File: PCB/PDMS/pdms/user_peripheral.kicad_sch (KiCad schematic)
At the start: 11 parts, among them IC12 TMP126NDCKR, IC14 TMP126NDCKR, Q2 MMBT3904

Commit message: Added connector and more
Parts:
- R56, R57: footprint (none) -> Resistor_SMD:R_0402_1005Metric
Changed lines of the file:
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@@
       (effects (font (size 1.27 1.27)) (justify left))
     )
-    (property "Footprint" "" (id 2) (at 59.055 57.785 0)
+    (property "Footprint" "Resistor_SMD:R_0402_1005Metric" (id 2) (at 59.055 57.785 0)
       (effects (font (size 1.27 1.27)) hide)
     )
@@
       (effects (font (size 1.27 1.27)) (justify left))
     )
-    (property "Footprint" "" (id 2) (at 135.255 57.785 0)
-      (effects (font (size 1.27 1.27)) hide)
-    )
+    (property "Footprint" "Resistor_SMD:R_0402_1005Metric" (id 2) (at 135.255 57.785 0)
+      (effects (font (size 1.27 1.27)) hide)
+    )

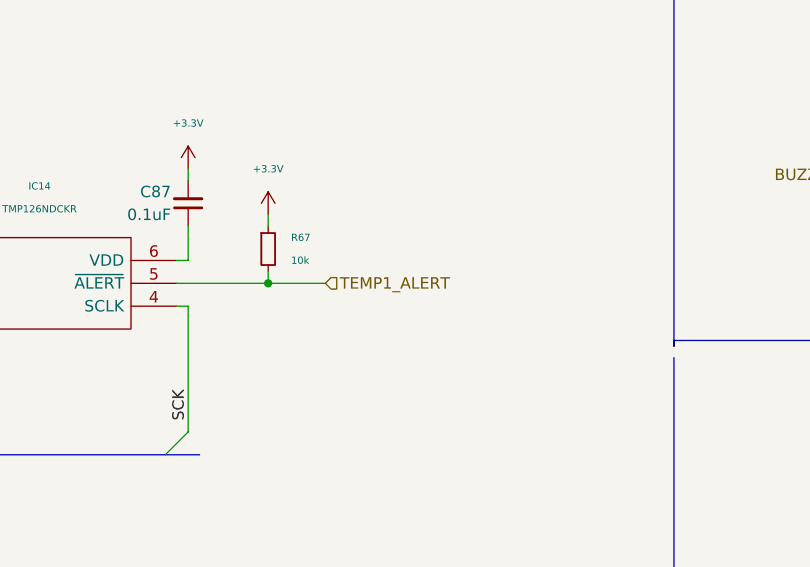
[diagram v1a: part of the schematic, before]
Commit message: Added voltage mux section & layouting high side - hp
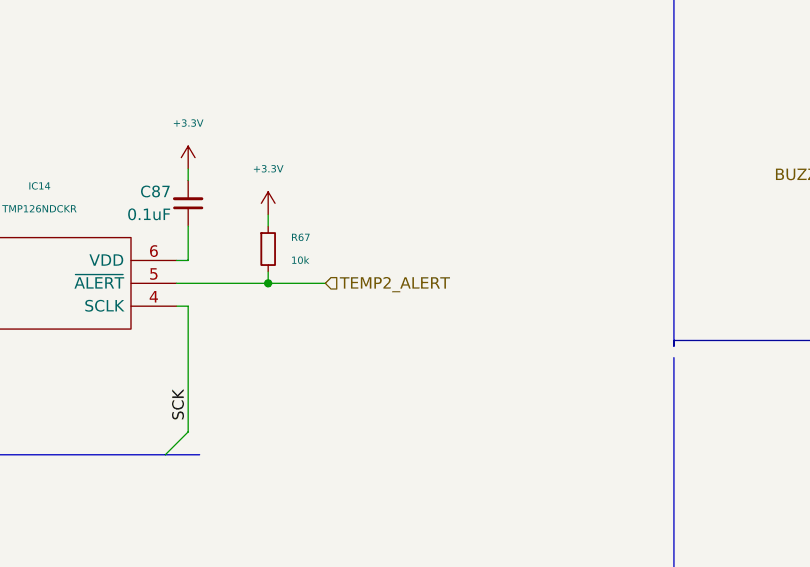
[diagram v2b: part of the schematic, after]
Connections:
- net TEMP1_ALERT: no longer IC14.5 (~{ALERT}), R67.2
- new net TEMP2_ALERT: IC14.5 (~{ALERT}), R67.2
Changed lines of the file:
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@@
     (effects (font (size 1.27 1.27)) (justify right))
   )
-  (hierarchical_label "TEMP1_ALERT" (shape input) (at 184.785 51.435 0)
+  (hierarchical_label "TEMP2_ALERT" (shape input) (at 184.785 51.435 0)
     (effects (font (size 1.27 1.27)) (justify left))
   )

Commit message: Flash layout
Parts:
- C86, C87: footprint Capacitor_SMD:C_0402_1005Metric_Pad0.74x0.62mm_HandSolder -> Capacitor_SMD:C_0402_1005Metric
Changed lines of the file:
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@@
       (effects (font (size 1.27 1.27)) (justify right))
     )
-    (property "Footprint" "Capacitor_SMD:C_0402_1005Metric_Pad0.74x0.62mm_HandSolder" (id 2) (at 169.545 42.545 0)
+    (property "Footprint" "Capacitor_SMD:C_0402_1005Metric" (id 2) (at 169.545 42.545 0)
       (effects (font (size 1.27 1.27)) hide)
     )
@@
       (effects (font (size 1.27 1.27)) (justify right))
     )
-    (property "Footprint" "Capacitor_SMD:C_0402_1005Metric_Pad0.74x0.62mm_HandSolder" (id 2) (at 93.345 42.545 0)
+    (property "Footprint" "Capacitor_SMD:C_0402_1005Metric" (id 2) (at 93.345 42.545 0)
       (effects (font (size 1.27 1.27)) hide)
     )

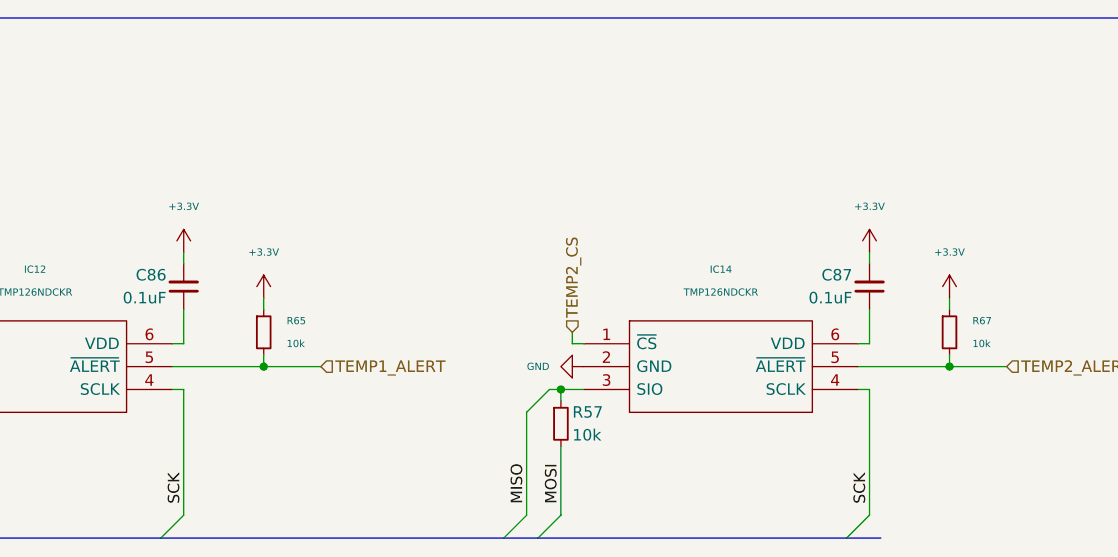
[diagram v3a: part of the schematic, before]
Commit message: ADC protection refactored - 73
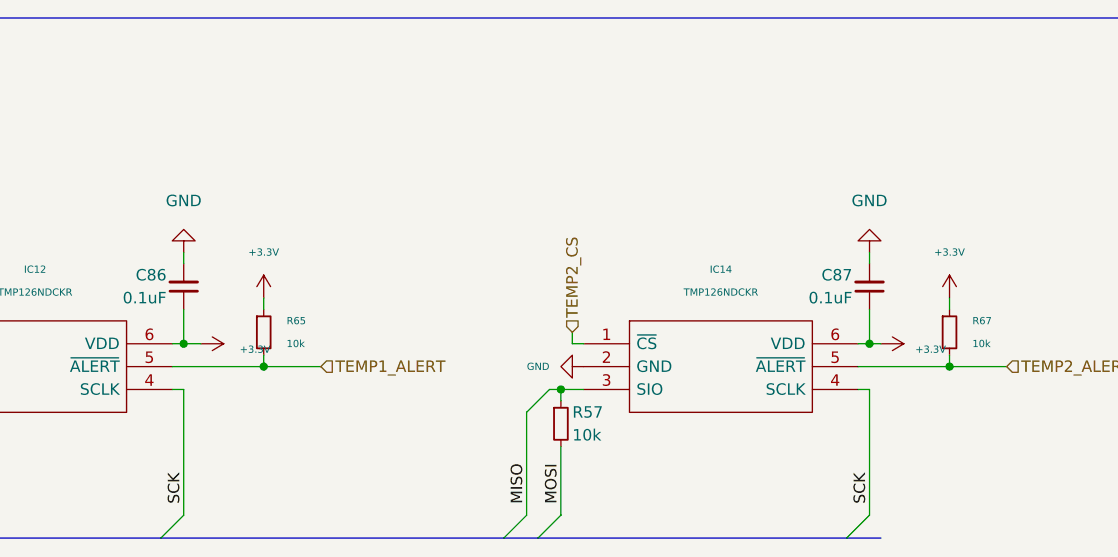
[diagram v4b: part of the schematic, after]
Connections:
- net +3.3V: now also C86.1, C87.1, IC12.6 (VDD), IC14.6 (VDD); no longer C86.2, C87.2
- net GND: now also C86.2, C87.2
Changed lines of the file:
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@@
   (junction (at 59.055 53.975) (diameter 0) (color 0 0 0 0)
   )
+  (junction (at 93.345 48.895) (diameter 0) (color 0 0 0 0)
+  )
   (junction (at 178.435 51.435) (diameter 0) (color 0 0 0 0)
   )
@@
   (junction (at 102.235 51.435) (diameter 0) (color 0 0 0 0)
   )
+  (junction (at 169.545 48.895) (diameter 0) (color 0 0 0 0)
+  )
   (bus_entry (at 128.905 70.485) (size 2.54 -2.54)
     (stroke (width 0) (type default) (color 0 0 0 0))
@@
     (stroke (width 0) (type default) (color 0 0 0 0))
   )
+  (wire (pts (xy 169.545 48.895) (xy 170.815 48.895))
+    (stroke (width 0) (type default) (color 0 0 0 0))
+  )
   (wire (pts (xy 102.235 51.435) (xy 108.585 51.435))
     (stroke (width 0) (type default) (color 0 0 0 0))
@@
   )
   (wire (pts (xy 93.345 53.975) (xy 93.345 67.945))
+    (stroke (width 0) (type default) (color 0 0 0 0))
+  )
+  (wire (pts (xy 93.345 48.895) (xy 95.25 48.895))
     (stroke (width 0) (type default) (color 0 0 0 0))
   )
@@
     (pin "2")
   )
+  (symbol (lib_id "power:GND") (at 169.545 38.735 180) (unit 1)
+    (in_bom yes) (on_board yes) (fields_autoplaced)
+    (property "Reference" "#PWR0309" (id 0) (at 169.545 32.385 0)
+      (effects (font (size 1.27 1.27)) hide)
+    )
+    (property "Value" "GND" (id 1) (at 169.545 33.02 0))
+    (property "Footprint" "" (id 2) (at 169.545 38.735 0)
+      (effects (font (size 1.27 1.27)) hide)
+    )
+    (property "Datasheet" "" (id 3) (at 169.545 38.735 0)
+      (effects (font (size 1.27 1.27)) hide)
+    )
+    (pin "1")
+  )
   (symbol (lib_id "Device:R_Small") (at 59.055 57.785 0) (unit 1)
     (in_bom yes) (on_board yes)
@@
     (pin "2")
   )
-  (symbol (lib_id "power:+3.3V") (at 93.345 38.735 0) (unit 1)
-    (in_bom yes) (on_board yes) (fields_autoplaced)
-    (property "Reference" "#PWR0194" (id 0) (at 93.345 42.545 0)
+  (symbol (lib_id "power:+3.3V") (at 95.25 48.895 270) (unit 1)
+    (in_bom yes) (on_board yes) (fields_autoplaced)
+    (property "Reference" "#PWR0194" (id 0) (at 91.44 48.895 0)
       (effects (font (size 0.8 0.8)) hide)
     )
-    (property "Value" "+3.3V" (id 1) (at 93.345 33.655 0)
-      (effects (font (size 0.8 0.8)))
-    )
+    (property "Value" "+3.3V" (id 1) (at 99.568 49.53 90)
+      (effects (font (size 0.8 0.8)) (justify left))
+    )
+    (property "Footprint" "" (id 2) (at 95.25 48.895 0)
+      (effects (font (size 1.27 1.27)) hide)
+    )
+    (property "Datasheet" "" (id 3) (at 95.25 48.895 0)
+      (effects (font (size 1.27 1.27)) hide)
+    )
+    (pin "1")
+  )
+  (symbol (lib_id "power:+3.3V") (at 170.815 48.895 270) (unit 1)
+    (in_bom yes) (on_board yes) (fields_autoplaced)
+    (property "Reference" "#PWR0233" (id 0) (at 167.005 48.895 0)
+      (effects (font (size 0.8 0.8)) hide)
+    )
+    (property "Value" "+3.3V" (id 1) (at 174.625 49.53 90)
+      (effects (font (size 0.8 0.8)) (justify left))
+    )
+    (property "Footprint" "" (id 2) (at 170.815 48.895 0)
+      (effects (font (size 1.27 1.27)) hide)
+    )
+    (property "Datasheet" "" (id 3) (at 170.815 48.895 0)
+      (effects (font (size 1.27 1.27)) hide)
+    )
+    (pin "1")
+  )
+  (symbol (lib_id "power:GND") (at 93.345 38.735 180) (unit 1)
+    (in_bom yes) (on_board yes) (fields_autoplaced)
+    (property "Reference" "#PWR0310" (id 0) (at 93.345 32.385 0)
+      (effects (font (size 1.27 1.27)) hide)
+    )
+    (property "Value" "GND" (id 1) (at 93.345 33.02 0))
     (property "Footprint" "" (id 2) (at 93.345 38.735 0)
       (effects (font (size 1.27 1.27)) hide)
@@
       (effects (font (size 1.27 1.27)) hide)
     )
-    (pin "1")
-  )
-  (symbol (lib_id "power:+3.3V") (at 169.545 38.735 0) (unit 1)
-    (in_bom yes) (on_board yes) (fields_autoplaced)
-    (property "Reference" "#PWR0233" (id 0) (at 169.545 42.545 0)
-      (effects (font (size 0.8 0.8)) hide)
-    )
-    (property "Value" "+3.3V" (id 1) (at 169.545 33.655 0)
-      (effects (font (size 0.8 0.8)))
-    )
-    (property "Footprint" "" (id 2) (at 169.545 38.735 0)
-      (effects (font (size 1.27 1.27)) hide)
-    )
-    (property "Datasheet" "" (id 3) (at 169.545 38.735 0)
-      (effects (font (size 1.27 1.27)) hide)
-    )

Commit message: PCB finished
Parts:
- removed Q2: MMBT3904, Package_TO_SOT_SMD:SOT-23, symbol Transistor_BJT:MMBT3904
- added Q2: RJU002N06FRAT106, PDMS_Additional:SOT65P210X110-3N, symbol BSPD-07:RJU002N06FRAT106
- BZ1: footprint Buzzer_Beeper:Buzzer_Murata_PKLCS1212E -> Buzzer_Beeper:Buzzer_12x9.5RM7.6
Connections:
- net GND: now also Q2.2
- net at R72.2: now also Q2.1
- net at BZ1.2 (+): now also Q2.3
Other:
- moved on the sheet: BZ1
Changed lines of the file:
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@@
     (stroke (width 0) (type default) (color 0 0 0 0))
   )
-  (wire (pts (xy 243.84 39.37) (xy 245.11 39.37))
+  (wire (pts (xy 243.84 39.624) (xy 245.11 39.624))
     (stroke (width 0) (type default) (color 0 0 0 0))
   )
@@
     (stroke (width 0) (type default) (color 0 0 0 0))
   )
-  (wire (pts (xy 259.08 25.4) (xy 259.08 26.67))
+  (wire (pts (xy 259.08 20.574) (xy 259.08 21.844))
     (stroke (width 0) (type default) (color 0 0 0 0))
   )
@@
     (stroke (width 0) (type default) (color 0 0 0 0))
   )
-  (wire (pts (xy 259.08 31.75) (xy 259.08 34.29))
-    (stroke (width 0) (type default) (color 0 0 0 0))
-  )
   (bus (pts (xy 128.905 70.485) (xy 132.715 70.485))
     (stroke (width 0) (type default) (color 0 0 0 0))
@@
     (stroke (width 0) (type default) (color 0 0 0 0))
   )
-  (wire (pts (xy 250.19 39.37) (xy 251.46 39.37))
+  (wire (pts (xy 250.19 39.624) (xy 251.46 39.624))
+    (stroke (width 0) (type default) (color 0 0 0 0))
+  )
+  (wire (pts (xy 259.08 26.924) (xy 259.08 29.464))
     (stroke (width 0) (type default) (color 0 0 0 0))
   )
@@
     (stroke (width 0) (type default) (color 0 0 0 0))
   )
+  (wire (pts (xy 259.08 44.704) (xy 259.08 48.26))
+    (stroke (width 0) (type default) (color 0 0 0 0))
+  )
   (wire (pts (xy 93.345 48.895) (xy 92.075 48.895))
     (stroke (width 0) (type default) (color 0 0 0 0))
@@
   )
   (polyline (pts (xy 12.065 92.075) (xy 12.065 12.7))
-    (stroke (width 0) (type default) (color 0 0 0 0))
-  )
-  (wire (pts (xy 259.08 44.45) (xy 259.08 48.26))
     (stroke (width 0) (type default) (color 0 0 0 0))
   )
@@
     (effects (font (size 1.27 1.27)) (justify left))
   )
-  (hierarchical_label "BUZZ_IN" (shape input) (at 243.84 39.37 180)
+  (hierarchical_label "BUZZ_IN" (shape input) (at 243.84 39.624 180)
     (effects (font (size 1.27 1.27)) (justify right))
   )
@@
     (effects (font (size 1.27 1.27)) (justify left))
   )
-  (symbol (lib_id "power:+5V") (at 259.08 25.4 0) (unit 1)
-    (in_bom yes) (on_board yes)
-    (property "Reference" "#PWR0200" (id 0) (at 259.08 29.21 0)
+  (symbol (lib_id "power:+5V") (at 259.08 20.574 0) (unit 1)
+    (in_bom yes) (on_board yes)
+    (property "Reference" "#PWR0200" (id 0) (at 259.08 24.384 0)
       (effects (font (size 0.8 0.8)) hide)
     )
-    (property "Value" "+5V" (id 1) (at 259.08 21.59 0)
-      (effects (font (size 0.8 0.8)))
-    )
-    (property "Footprint" "" (id 2) (at 259.08 25.4 0)
-      (effects (font (size 0.6 0.6)) hide)
-    )
-    (property "Datasheet" "" (id 3) (at 259.08 25.4 0)
+    (property "Value" "+5V" (id 1) (at 259.08 16.764 0)
+      (effects (font (size 0.8 0.8)))
+    )
+    (property "Footprint" "" (id 2) (at 259.08 20.574 0)
+      (effects (font (size 0.6 0.6)) hide)
+    )
+    (property "Datasheet" "" (id 3) (at 259.08 20.574 0)
       (effects (font (size 0.6 0.6)) hide)
     )
@@
     (pin "1")
     (pin "2")
+  )
+  (symbol (lib_id "BSPD-07:RJU002N06FRAT106") (at 251.46 39.624 0) (unit 1)
+    (in_bom yes) (on_board yes)
+    (property "Reference" "Q2" (id 0) (at 263.652 38.1 90))
+    (property "Value" "RJU002N06FRAT106" (id 1) (at 266.192 38.1 90)
+      (effects (font (size 0.8 0.8)))
+    )
+    (property "Footprint" "PDMS_Additional:SOT65P210X110-3N" (id 2) (at 262.89 40.894 0)
+      (effects (font (size 1.27 1.27)) (justify left) hide)
+    )
+    (property "Datasheet" "https://datasheet.datasheetarchive.com/originals/distributors/DKDS-10/185695.pdf" (id 3) (at 262.89 43.434 0)
+      (effects (font (size 1.27 1.27)) (justify left) hide)
+    )
+    (property "Description" "ROHM - RJU002N06FRAT106 - MOSFET, AEC-Q101, N-CH, 60V, 0.2A, UMT3" (id 4) (at 262.89 45.974 0)
+      (effects (font (size 1.27 1.27)) (justify left) hide)
+    )
+    (property "Height" "1" (id 5) (at 262.89 48.514 0)
+      (effects (font (size 1.27 1.27)) (justify left) hide)
+    )
+    (property "Manufacturer_Name" "ROHM Semiconductor" (id 6) (at 262.89 51.054 0)
+      (effects (font (size 1.27 1.27)) (justify left) hide)
+    )
+    (property "Manufacturer_Part_Number" "RJU002N06FRAT106" (id 7) (at 262.89 53.594 0)
+      (effects (font (size 1.27 1.27)) (justify left) hide)
+    )
+    (property "Mouser Part Number" "755-RJU002N06FRAT106" (id 8) (at 262.89 56.134 0)
+      (effects (font (size 1.27 1.27)) (justify left) hide)
+    )
+    (property "Mouser Price/Stock" "https://www.mouser.com/Search/Refine.aspx?Keyword=755-RJU002N06FRAT106" (id 9) (at 262.89 58.674 0)
+      (effects (font (size 1.27 1.27)) (justify left) hide)
+    )
+    (property "Arrow Part Number" "" (id 10) (at 262.89 61.214 0)
+      (effects (font (size 1.27 1.27)) (justify left) hide)
+    )
+    (property "Arrow Price/Stock" "" (id 11) (at 262.89 63.754 0)
+      (effects (font (size 1.27 1.27)) (justify left) hide)
+    )
+    (property "Mouser Testing Part Number" "" (id 12) (at 262.89 66.294 0)
+      (effects (font (size 1.27 1.27)) (justify left) hide)
+    )
+    (property "Mouser Testing Price/Stock" "" (id 13) (at 262.89 68.834 0)
+      (effects (font (size 1.27 1.27)) (justify left) hide)
+    )
+    (pin "1")
+    (pin "2")
+    (pin "3")
   )
   (symbol (lib_id "power:+3.3V") (at 95.25 48.895 270) (unit 1)
@@
     (pin "6")
   )
-  (symbol (lib_id "Transistor_BJT:MMBT3904") (at 256.54 39.37 0) (unit 1)
-    (in_bom yes) (on_board yes)
-    (property "Reference" "Q2" (id 0) (at 261.62 38.0999 0)
-      (effects (font (size 0.8 0.8)) (justify left))
-    )
-    (property "Value" "MMBT3904" (id 1) (at 261.62 39.37 0)
-      (effects (font (size 0.8 0.8)) (justify left))
-    )
-    (property "Footprint" "Package_TO_SOT_SMD:SOT-23" (id 2) (at 261.62 41.275 0)
-      (effects (font (size 0.6 0.6) italic) (justify left) hide)
-    )
-    (property "Datasheet" "https://www.onsemi.com/pub/Collateral/2N3903-D.PDF" (id 3) (at 256.54 39.37 0)
-      (effects (font (size 0.6 0.6)) (justify left) hide)
-    )
-    (pin "1")
-    (pin "2")
-    (pin "3")
-  )
   (symbol (lib_id "Device:C_Small") (at 93.345 42.545 0) (mirror x) (unit 1)
     (in_bom yes) (on_board yes)
@@
     (pin "2")
   )
-  (symbol (lib_id "Device:Buzzer") (at 261.62 29.21 0) (unit 1)
-    (in_bom yes) (on_board yes)
-    (property "Reference" "BZ1" (id 0) (at 265.43 27.9399 0)
-      (effects (font (size 0.8 0.8)) (justify left))
-    )
-    (property "Value" "Buzzer" (id 1) (at 265.43 29.21 0)
-      (effects (font (size 0.8 0.8)) (justify left))
-    )
-    (property "Footprint" "Buzzer_Beeper:Buzzer_Murata_PKLCS1212E" (id 2) (at 260.985 26.67 90)
-      (effects (font (size 0.6 0.6)) hide)
-    )
-    (property "Datasheet" "~" (id 3) (at 260.985 26.67 90)
-      (effects (font (size 0.6 0.6)) hide)
-    )
-    (pin "1")
-    (pin "2")
-  )
-  (symbol (lib_id "Device:R_Small") (at 247.65 39.37 90) (unit 1)
-    (in_bom yes) (on_board yes)
-    (property "Reference" "R72" (id 0) (at 247.65 39.37 90)
-      (effects (font (size 0.8 0.8)))
-    )
-    (property "Value" "1k" (id 1) (at 247.65 38.1 90)
-      (effects (font (size 0.8 0.8)))
-    )
-    (property "Footprint" "Resistor_SMD:R_0402_1005Metric" (id 2) (at 247.65 39.37 0)
-      (effects (font (size 0.6 0.6)) hide)
-    )
-    (property "Datasheet" "~" (id 3) (at 247.65 39.37 0)
-      (effects (font (size 0.6 0.6)) hide)
-    )
+  (symbol (lib_id "Device:Buzzer") (at 261.62 24.384 0) (unit 1)
+    (in_bom yes) (on_board yes)
+    (property "Reference" "BZ1" (id 0) (at 265.43 23.1139 0)
+      (effects (font (size 0.8 0.8)) (justify left))
+    )
+    (property "Value" "Buzzer" (id 1) (at 265.43 24.384 0)
+      (effects (font (size 0.8 0.8)) (justify left))
+    )
+    (property "Footprint" "Buzzer_Beeper:Buzzer_12x9.5RM7.6" (id 2) (at 260.985 21.844 90)
+      (effects (font (size 0.6 0.6)) hide)
+    )
+    (property "Datasheet" "~" (id 3) (at 260.985 21.844 90)
+      (effects (font (size 0.6 0.6)) hide)
+    )
+    (pin "1")
+    (pin "2")
+  )
+  (symbol (lib_id "Device:R_Small") (at 247.65 39.624 90) (unit 1)
+    (in_bom yes) (on_board yes)
+    (property "Reference" "R72" (id 0) (at 247.65 39.624 90)
+      (effects (font (size 0.8 0.8)))
+    )
+    (property "Value" "1k" (id 1) (at 247.65 38.354 90)
+      (effects (font (size 0.8 0.8)))
+    )
+    (property "Footprint" "Resistor_SMD:R_0402_1005Metric" (id 2) (at 247.65 39.624 0)
+      (effects (font (size 0.6 0.6)) hide)
+    )
+    (property "Datasheet" "~" (id 3) (at 247.65 39.624 0)
+      (effects (font (size 0.6 0.6)) hide)
+    )
